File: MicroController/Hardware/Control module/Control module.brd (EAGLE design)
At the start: 100 x 80 mm, 27 parts, among them Q1 BSS138, Q2 BSS138, Q3 BSS138, Q4 BSS138, Q5 BSS138, Q6 BSS138, Q7 BSS138, Q8 BSS138, U1 CD74HC4067SM96

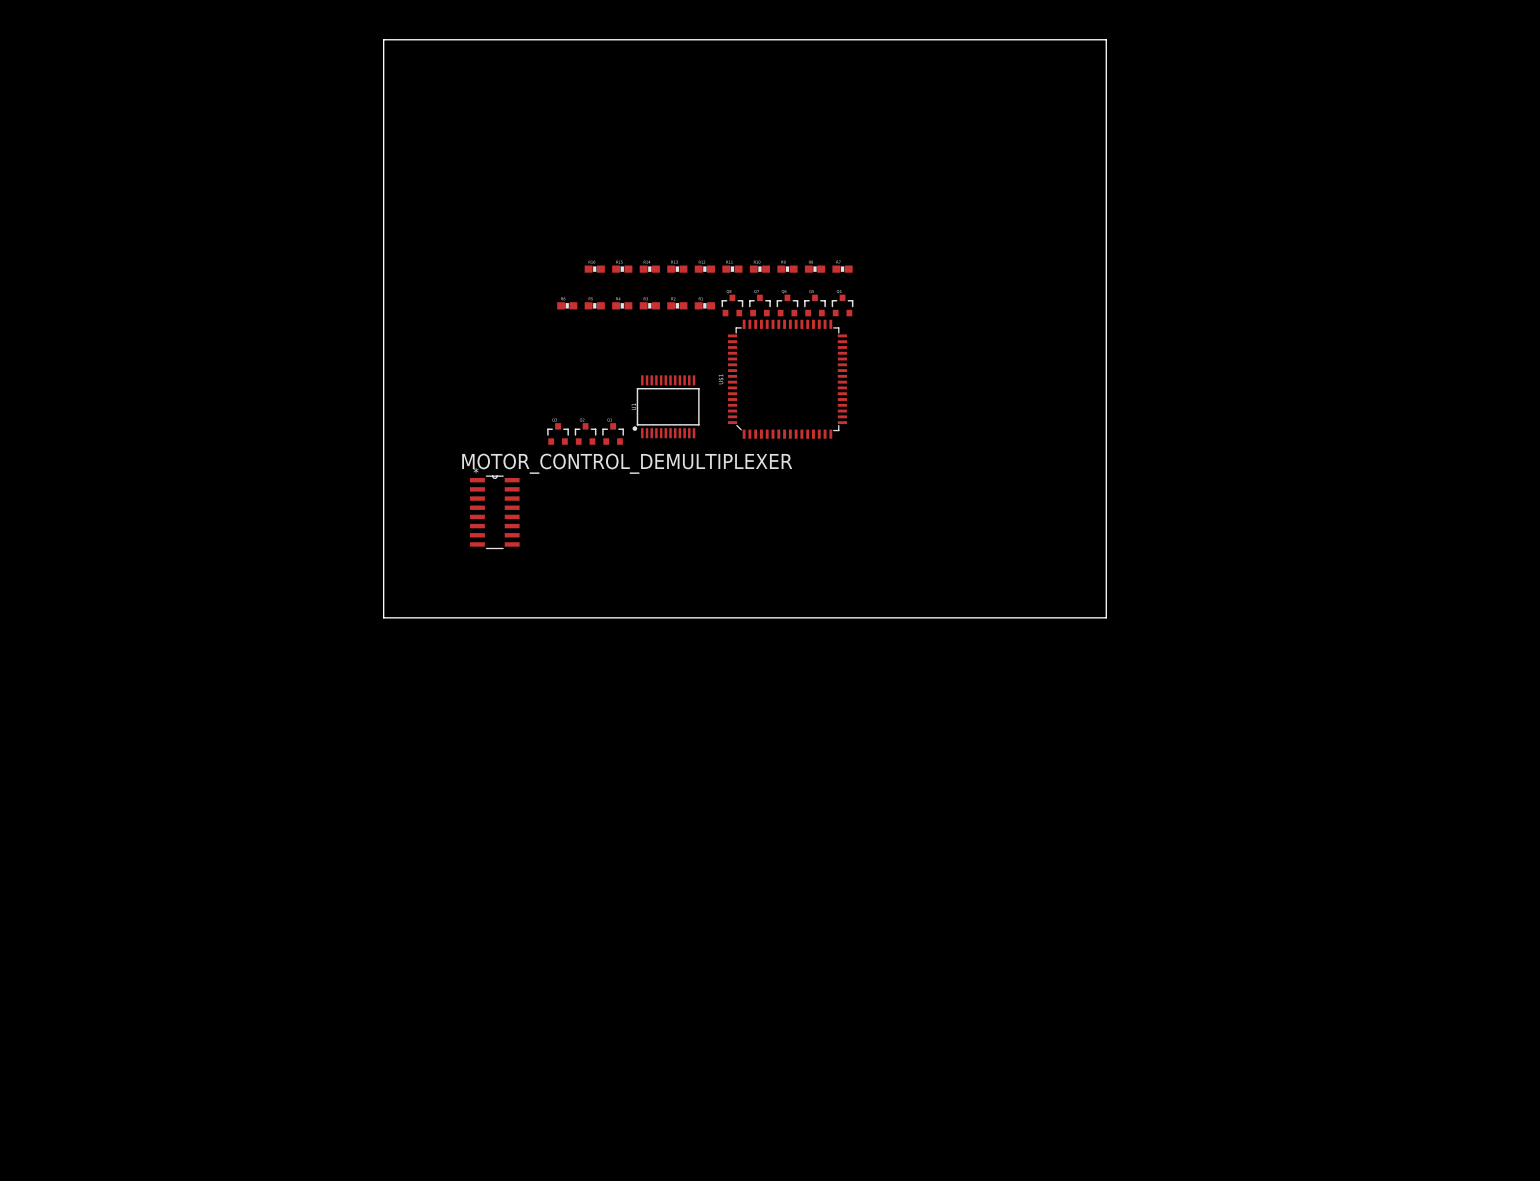
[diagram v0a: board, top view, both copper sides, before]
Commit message: Editted the board file and added power regulating components
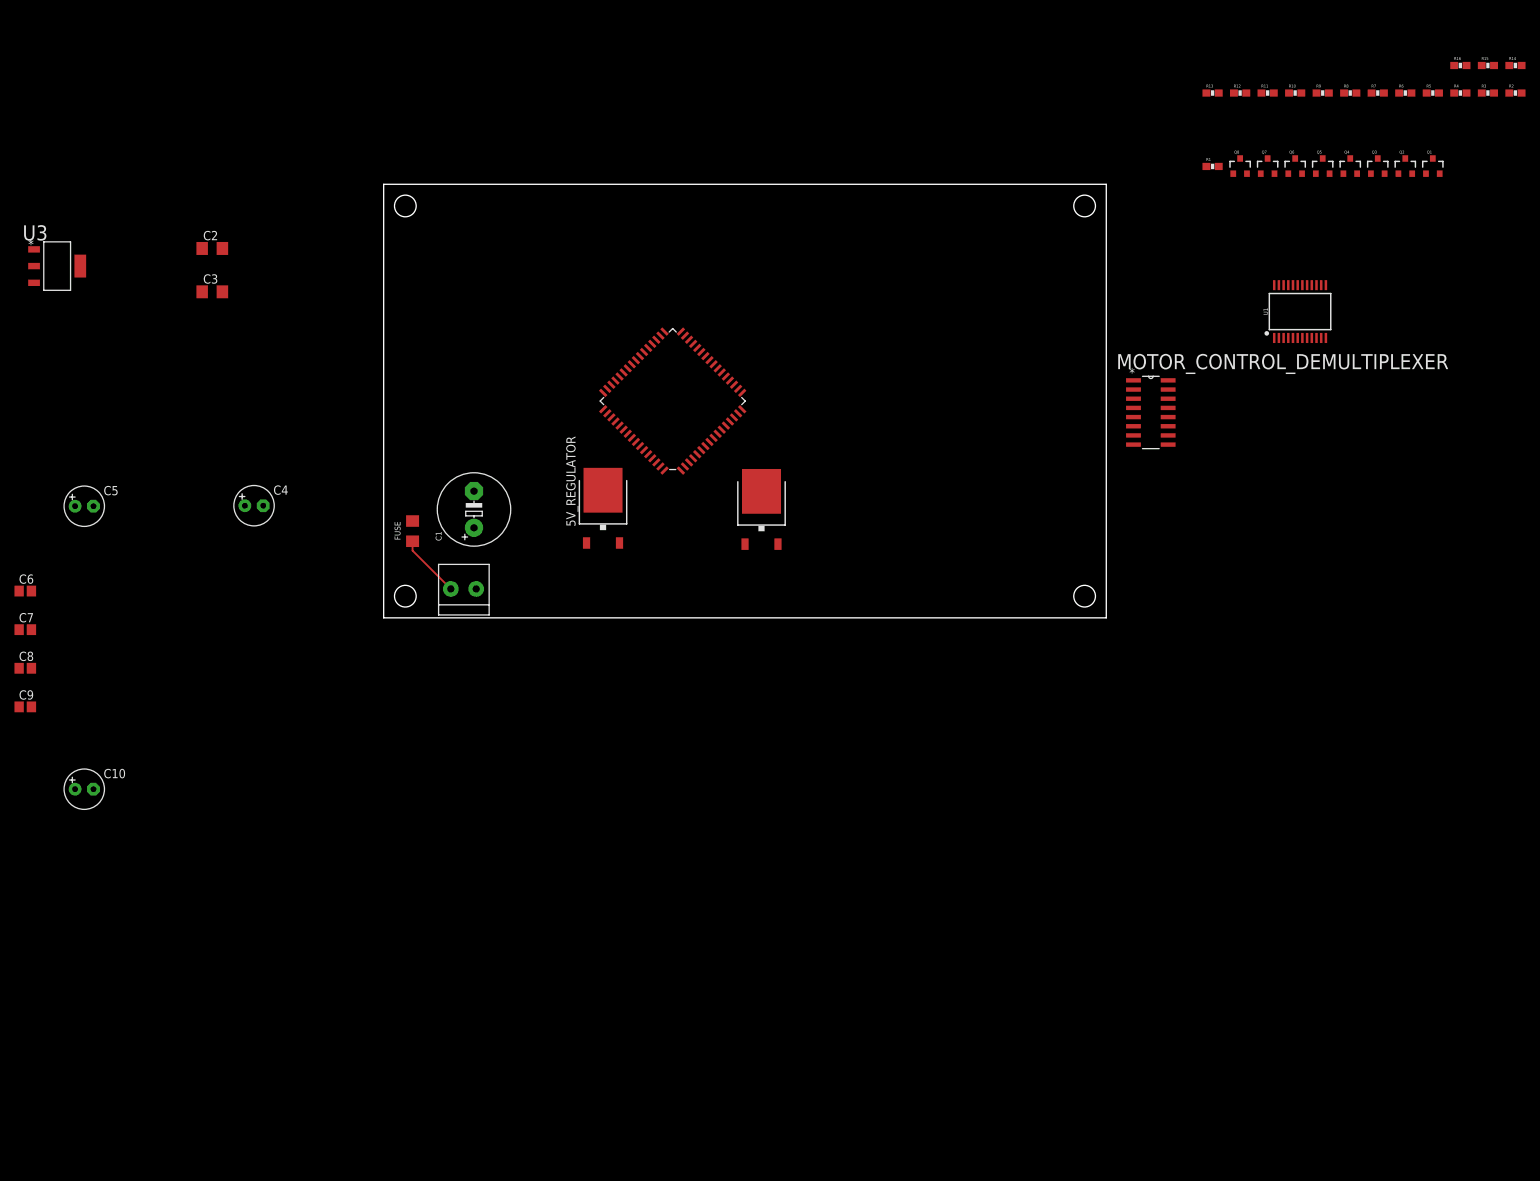
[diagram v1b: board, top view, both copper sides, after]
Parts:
- added 12V_REGULATOR: 7812DT, adafruit:TO252
- added 5V_REGULATOR: 7805DT, adafruit:TO252
- added C1: (no value), adafruit:E5-10,5
- added C10, C4, C5: (no value), adafruit:E2,5-6
- added C2, C3: (no value), adafruit:C1206
- added C6, C7, C8, C9: (no value), adafruit:C0805
- added FUSE: 6V/0.5A, SparkFun-Fuses:1206
- added J1: 1X2-3.5MM, adafruit:1X2-3.5MM
- added U3: TLV1117-33CDCY, Texas Instruments_By_element14_Batch_1:SOT230P700X180-4N
- moved R15 123.1 mm to (152.8, 76.4)
- moved R16 123.1 mm to (149.0, 76.4)
- moved R14 123.1 mm to (156.6, 76.4)
- moved R3 119.7 mm to (152.8, 72.6)
- moved R4 119.7 mm to (149.0, 72.6)
- moved R5 119.7 mm to (145.2, 72.6)
- moved R6 119.7 mm to (141.4, 72.6)
- moved R2 119.7 mm to (156.6, 72.6)
- moved Q1 119.3 mm to (145.2, 62.5)
- moved Q2 119.3 mm to (141.4, 62.5)
- moved Q3 119.3 mm to (137.6, 62.5)
- moved MOTOR_CONTROL_DEMULTIPLEXER 91.8 mm to (108.6, 24.0)
- moved U1 88.4 mm to (126.8, 42.4)
- moved R10 78.0 mm to (126.1, 72.6)
- moved R11 78.0 mm to (122.3, 72.6)
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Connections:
- removed net HV: R10.1, R12.1, R14.1, R16.1, R3.1, R5.1, R6.1, R8.1
- removed net LV: Q1.1, Q2.1, Q3.1, Q4.1, Q5.1, Q6.1, Q7.1, Q8.1, R1.1, R11.1, R13.1, R15.1, R2.1, R4.1, R7.1, R9.1
- new net +12V: 12V_REGULATOR.2, C4.+, C6.1, C8.1, R10.1, R12.1, R14.1, R16.1, R3.1, R5.1, R6.1, R8.1, U3.3
- new net +24V: 12V_REGULATOR.1, 5V_REGULATOR.1, C1.+, C2.1, C3.1, FUSE.2
- new net +5V: 5V_REGULATOR.2, C5.+, C7.1
- new net VIN: FUSE.1, J1.2
- net GND: now also 12V_REGULATOR.3, 5V_REGULATOR.3, C1.-, C10.-, C2.2, C3.2, C4.-, C5.-, C6.2, C7.2, C8.2, C9.2, J1.1, U3.1
- net VCC: now also C10.+, C9.1, Q1.1, Q2.1, Q3.1, Q4.1, Q5.1, Q6.1, Q7.1, Q8.1, R1.1, R11.1, R13.1, R15.1, R2.1, R4.1, R7.1, R9.1, U3.2, U3.4
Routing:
- net VIN: track 0.00 -> 8.80 mm
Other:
- board size 100 x 80 mm -> 100 x 60 mm

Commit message: Power regulation implemented on the board design
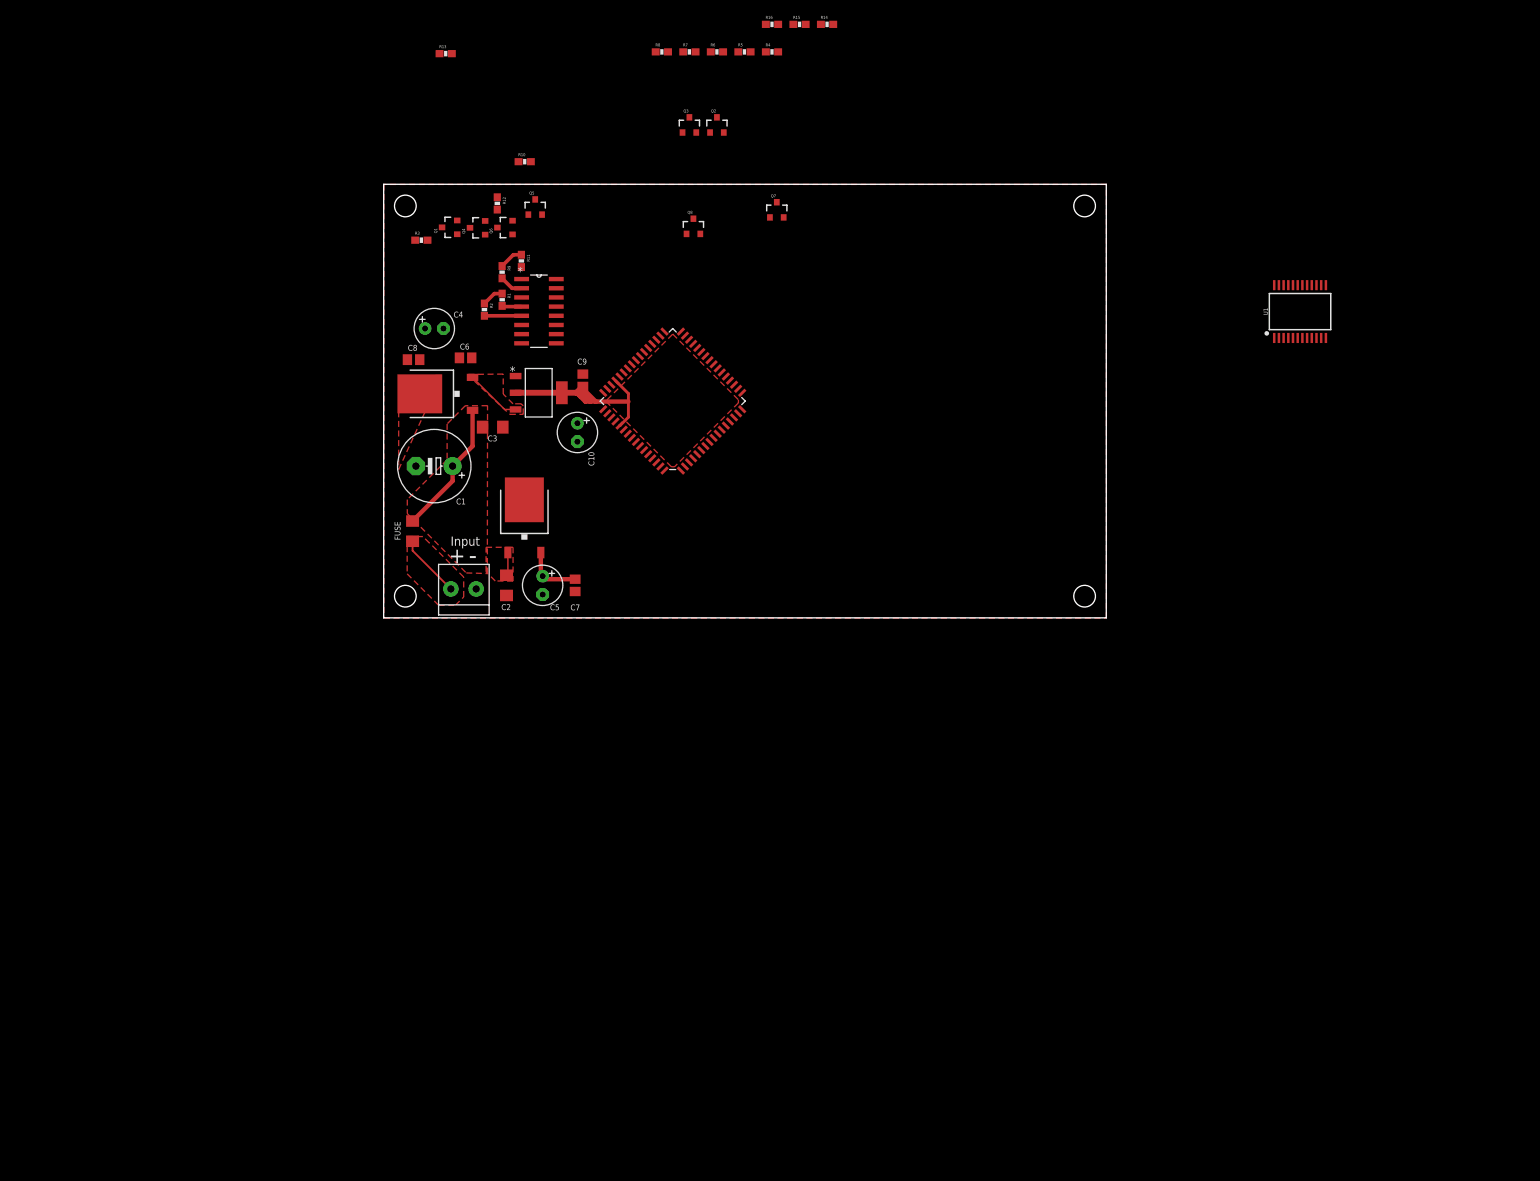
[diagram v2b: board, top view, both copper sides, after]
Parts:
- moved R3 149.0 mm to (5.21, 52.3)
- moved R2 145.8 mm to (13.9, 42.6), turned to 270 degrees
- moved Q1 136.3 mm to (9.18, 54.0), turned to 90 degrees
- moved Q4 121.0 mm to (13.0, 54.0), turned to 90 degrees
- moved R9 116.2 mm to (16.4, 47.8), turned to 270 degrees
- moved Q6 109.6 mm to (16.8, 54.0), turned to 90 degrees
- moved Q5 109.1 mm to (21.0, 56.8)
- moved R10 107.0 mm to (19.5, 63.1)
- moved R13 106.3 mm to (8.59, 78.1)
- moved R11 105.9 mm to (19.1, 49.4), turned to 270 degrees
- moved R12 103.9 mm to (15.7, 57.4), turned to 270 degrees
- moved R1 100.0 mm to (16.4, 44.0), turned to 270 degrees
- moved Q2 95.4 mm to (46.1, 68.2)
- moved Q3 95.4 mm to (42.3, 68.2)
- moved R15 95.4 mm to (57.5, 82.1)
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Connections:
- removed net VEE: MOTOR_CONTROL_DEMULTIPLEXER.8
- removed net VSS: MOTOR_CONTROL_DEMULTIPLEXER.7
- new net A: MOTOR_CONTROL_DEMULTIPLEXER.11
- new net B: MOTOR_CONTROL_DEMULTIPLEXER.10
- new net C: MOTOR_CONTROL_DEMULTIPLEXER.9
- net GND: now also MOTOR_CONTROL_DEMULTIPLEXER.6, MOTOR_CONTROL_DEMULTIPLEXER.7, MOTOR_CONTROL_DEMULTIPLEXER.8
- net VCC: now also MOTOR_CONTROL_DEMULTIPLEXER.16
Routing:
- net VCC: track 0.00 -> 38.1 mm
- net +24V: track 0.00 -> 22.1 mm
- net +5V: track 0.00 -> 8.69 mm
- net +12V: track 0.00 -> 7.80 mm
- net MOTOR_LEVEL_6: track 0.00 -> 5.15 mm
- net MOTOR_LEVEL_7: track 0.00 -> 3.27 mm
- net MOTOR_LEVEL_8: track 0.00 -> 2.79 mm
- added copper zone on layer 1, net +12V
- added copper zone on layer 1, net +24V
- added copper zone on layer 1, net GND
- added copper zone on layer 1, net VCC
- added copper zone on layer 1, net VIN
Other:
- board text added: "+"
- board text added: "-"
- board text added: "Input"

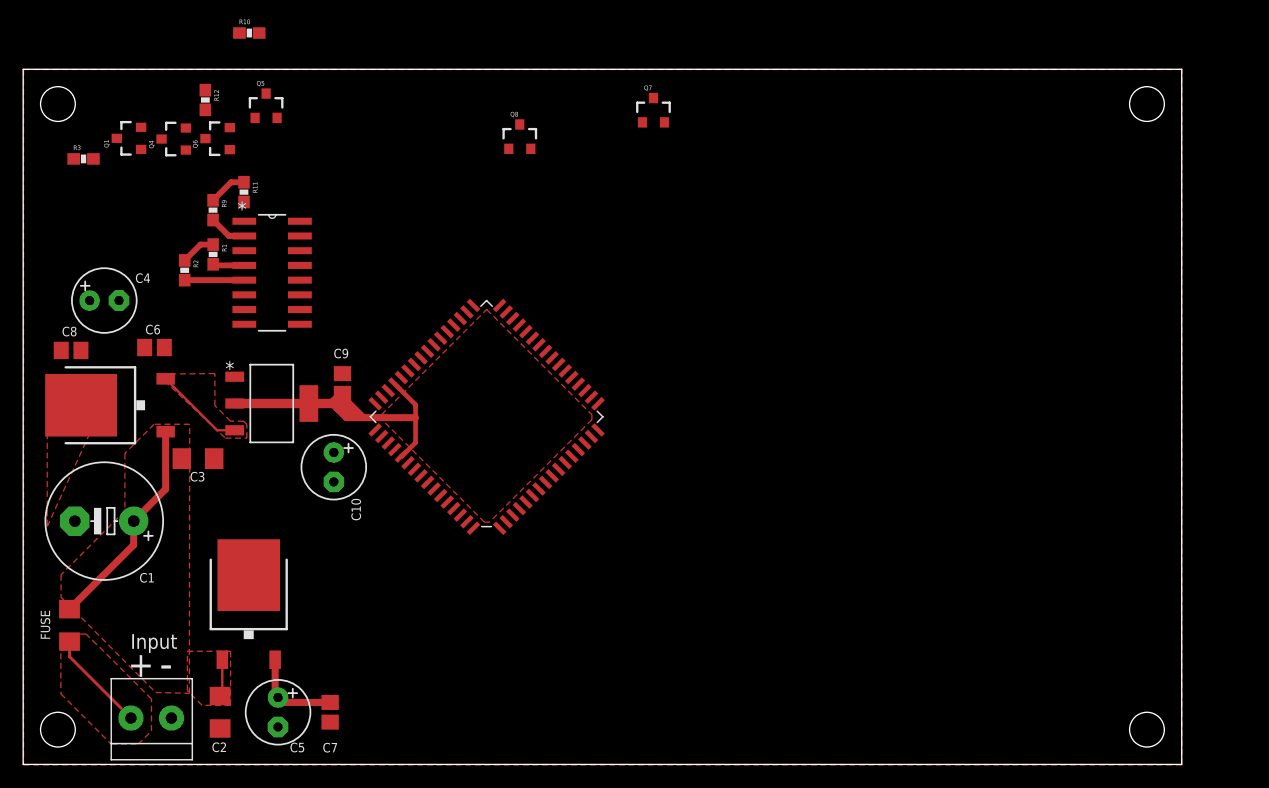
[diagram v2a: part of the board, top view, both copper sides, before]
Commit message: Removed some power lines and added the IR sensor connectors
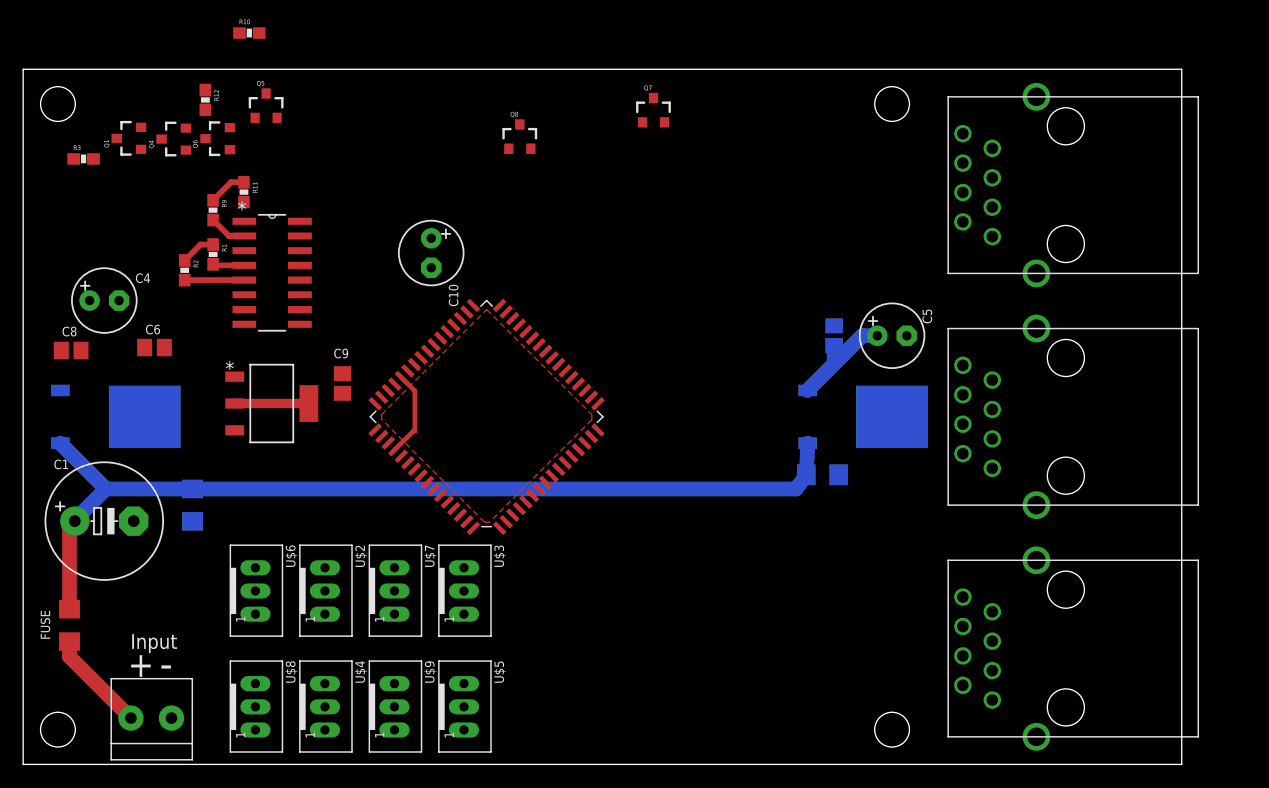
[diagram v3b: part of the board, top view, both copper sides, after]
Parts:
- added J2, J3, J4: RJ45-TRAFO, con-amphenol-rj45-ld:RJ45-TRAFO
- added U$2, U$3, U$4, U$5, U$6, U$7, U$8, U$9: JST-PH_3-PIN_HEADER, SRG:JST_B3B-PH_HEADER
- moved C5 62.2 mm to (75.0, 37.0), turned to 0 degrees
- moved 5V_REGULATOR 55.4 mm to (72.5, 30.0), flipped to the bottom, turned to 90 degrees
- moved C7 54.3 mm to (70.0, 37.0), flipped to the bottom, turned to 90 degrees
- moved C3 53.9 mm to (69.0, 25.0), flipped to the bottom, turned to 180 degrees
- moved C10 20.3 mm to (35.2, 44.1)
- moved C2 18.0 mm to (14.6, 22.4), flipped to the bottom
- moved 12V_REGULATOR 1.12 mm to (8.00, 30.0), flipped to the bottom
- turned C1 to 0 degrees
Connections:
- new net IR_1: U$6.P2
- new net IR_2: U$2.P2
- new net IR_3: U$7.P2
- new net IR_4: U$3.P2
- new net IR_5: U$8.P2
- new net IR_6: U$4.P2
- new net IR_7: U$9.P2
- new net IR_8: U$5.P2
- net GND: now also J2.8, J2.GND1, J2.GND2, J3.8, J3.GND1, J3.GND2, J4.8, J4.GND1, J4.GND2, U$2.P3, U$3.P3, U$4.P3, U$5.P3, U$6.P3, U$7.P3, U$8.P3, U$9.P3
- net VCC: now also U$2.P1, U$3.P1, U$4.P1, U$5.P1, U$6.P1, U$7.P1, U$8.P1, U$9.P1
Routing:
- net +24V: track 22.1 -> 81.1 mm
- net VCC: track 38.1 -> 12.7 mm
- net +12V: track 7.80 -> 0.00 mm
- net GND: track 0.00 -> 7.49 mm
- net +5V: track 8.69 -> 9.56 mm
- removed copper zone on layer 1, net +12V
- removed copper zone on layer 1, net +24V
- removed copper zone on layer 1, net VCC
- removed copper zone on layer 1, net VIN

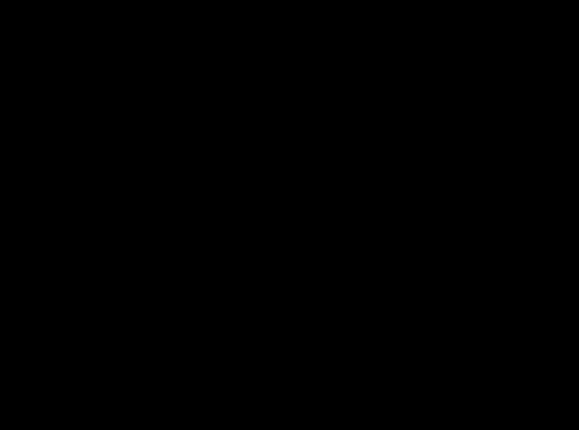
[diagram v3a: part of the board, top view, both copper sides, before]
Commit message: Looked into motor drivers and changed some components
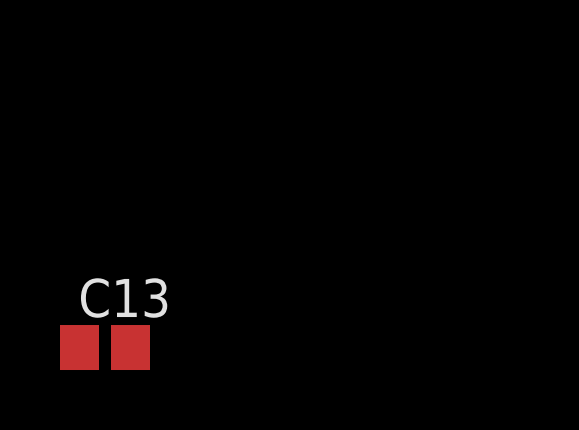
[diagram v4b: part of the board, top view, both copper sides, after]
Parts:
- added C13: (no value), adafruit:C0805
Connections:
- new net ULTRA10: U1.22
- new net ULTRA11: U1.21
- new net ULTRA12: U1.20
- new net ULTRA13: U1.19
- new net ULTRA14: U1.18
- new net ULTRA15: U1.17
- new net ULTRA16: U1.16
- new net ULTRA3: U1.7
- new net ULTRA4: U1.6
- new net ULTRA5: U1.5
- new net ULTRA6: U1.4
- new net ULTRA7: U1.3
- new net ULTRA8: U1.2
- new net ULTRA9: U1.23
- net GND: now also U$1.60, U1.12, U1.15
- net VCC: now also U$1.61, U1.24
